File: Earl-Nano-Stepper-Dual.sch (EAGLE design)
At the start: 25 parts, among them IC1 ULN2003AN, J4 CONNECTOR-M03254-LOCK, M1 ARDUINO-NANO-3.0, SW1 PB1, SW2 PB2, SW3 Toggle 1

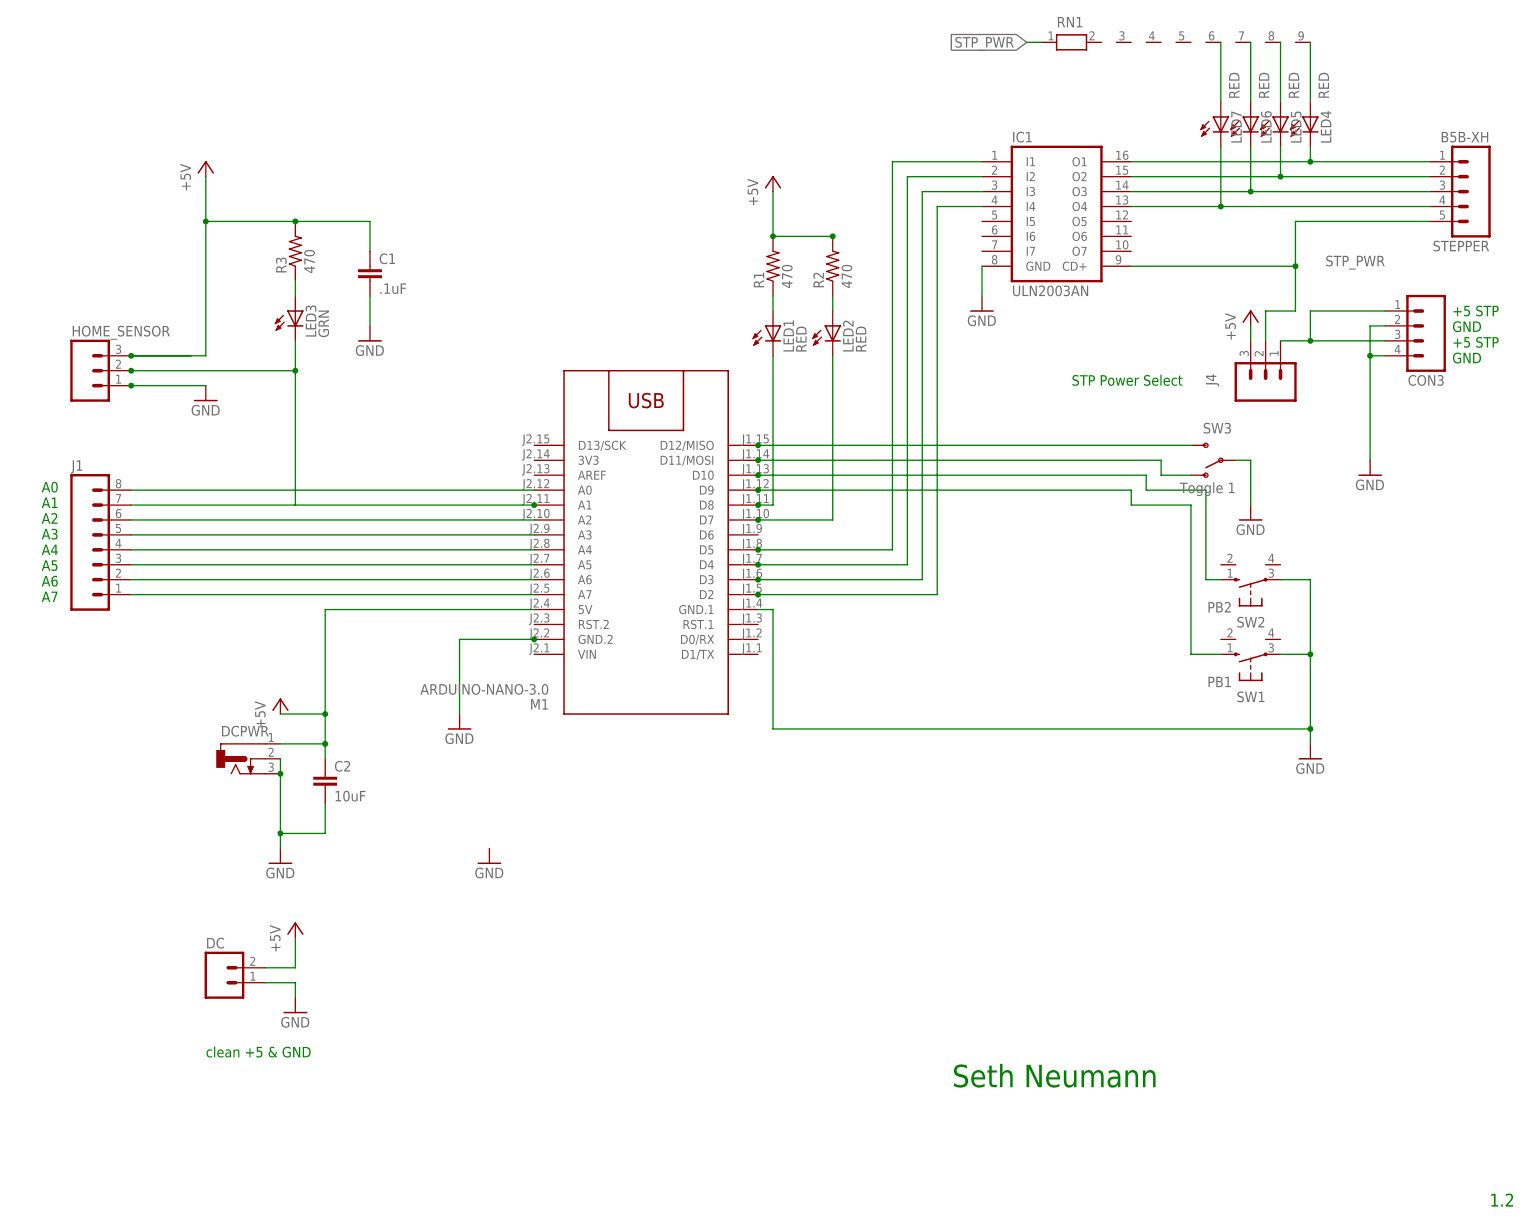
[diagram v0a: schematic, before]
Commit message: changes to support two stepper motors
changed to ULN2803
Moved both home sensors to A6,A7
Added LEDs, 2nd connector etc
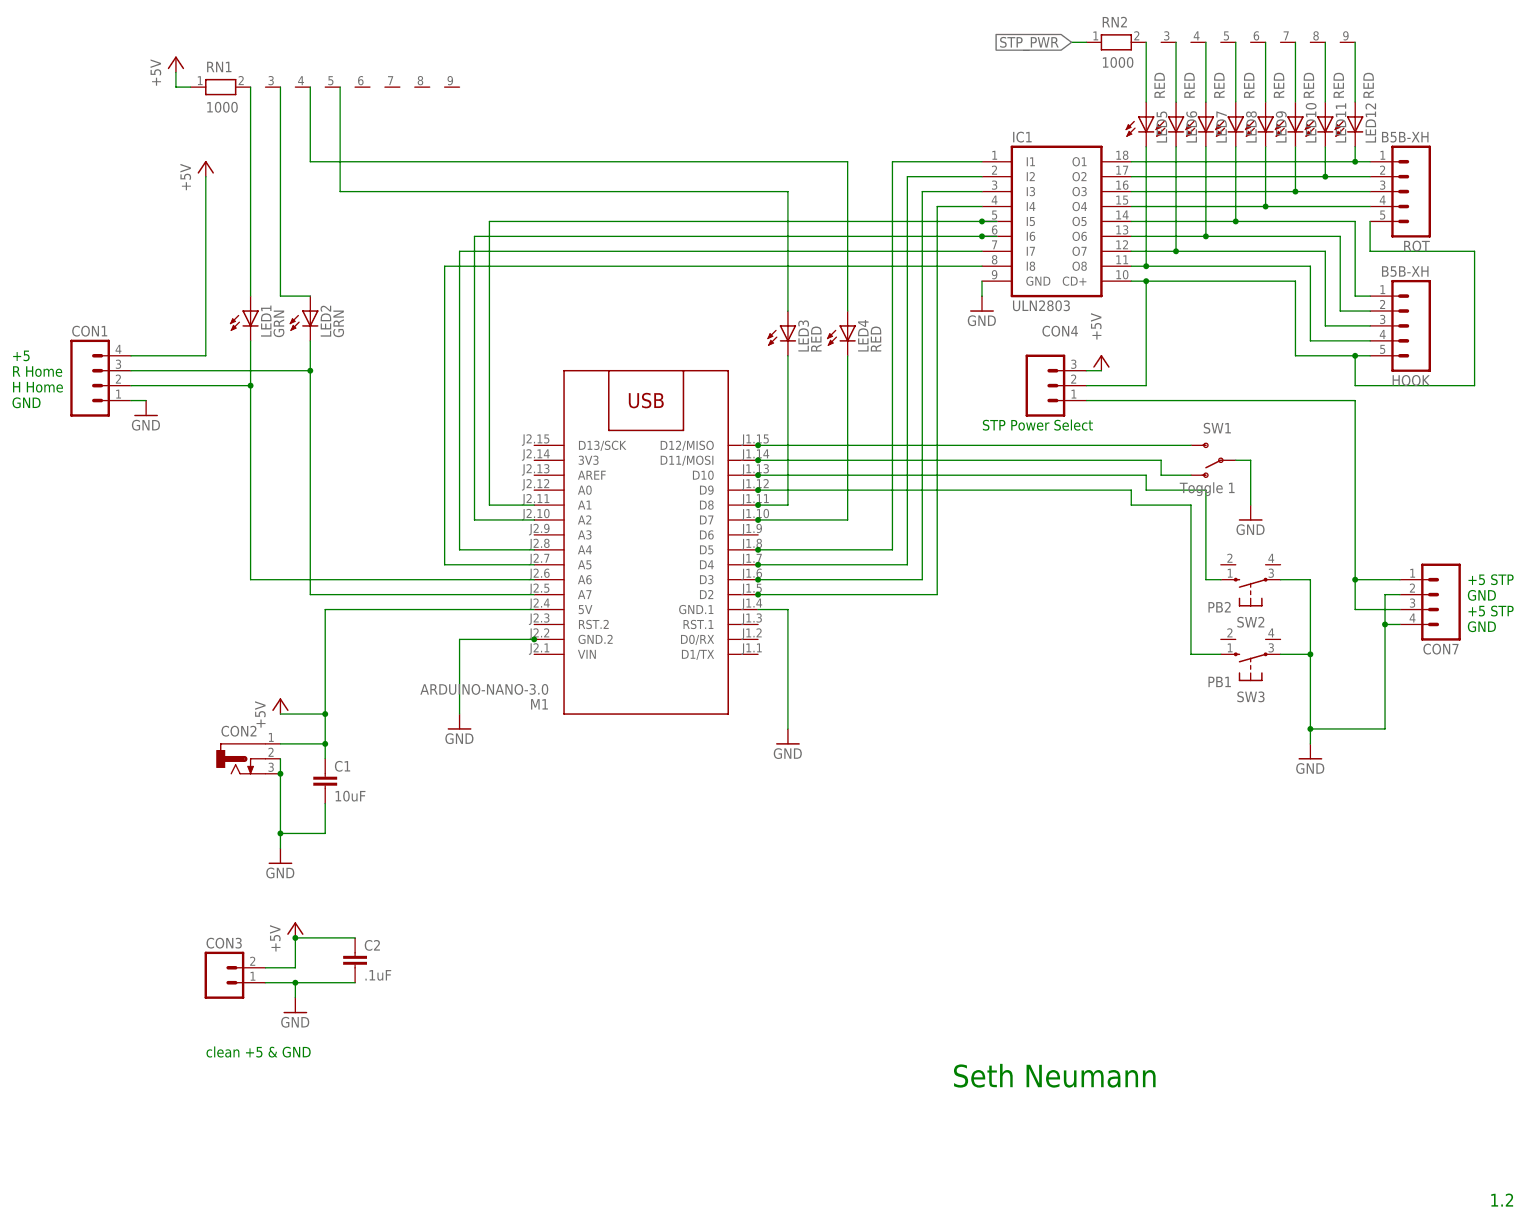
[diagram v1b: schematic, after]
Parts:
- removed DC: (no value), SPCoast:CONNECTOR-M02350-LOCK
- removed HOME_SENSOR, J4: CONNECTOR-M03254-LOCK, SPCoast:CONNECTOR-M03254-LOCK
- removed J1: (no value), SPCoast:CONNECTOR-M08LOCK
- removed R1, R2, R3: 470, SPCoast:RPTH04
- removed STEPPER: B5B-XH, SPCoast:CONNECTOR-M05LOCK
- added CON1: (no value), SPCoast:CONNECTOR-M04LOCK
- added CON4: CONNECTOR-M03254-LOCK, SPCoast:CONNECTOR-M03254-LOCK
- added CON7: (no value), SPCoast:CONNECTOR-M04SCREW_LOCK
- added HOOK, ROT: B5B-XH, SPCoast:CONNECTOR-M05LOCK
- added LED10, LED11, LED12, LED8, LED9: RED, SPCoast:LEDLED3MM
- added RN2: 1000, resistor-net:RN08
- C1: value .1uF -> 10uF
- C2: value 10uF -> .1uF
- CON3: device SPCoast:CONNECTOR-M04SCREW_LOCK -> SPCoast:CONNECTOR-M02350-LOCK
- IC1: value ULN2003AN -> ULN2803; device uln-udn:ULN2003AN -> uln-udn:ULN2803A
- LED1, LED2: value RED -> GRN
- LED3: value GRN -> RED
- RN1: value (none) -> 1000
- SW1: value PB1 -> Toggle 1; device SPCoast:SWITCH-(ON)SMALLPADS -> SPCoast:SWITCH-SPSTPTH-508
- SW3: value Toggle 1 -> PB1; device SPCoast:SWITCH-SPSTPTH-508 -> SPCoast:SWITCH-(ON)SMALLPADS
- renumbered DCPWR to CON2
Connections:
- removed net A1: HOME_SENSOR.2, J1.7, LED3.C, M1.A1
- new net N$28: CON4.1, CON7.1, CON7.3
- new net N$31: LED6.A, RN2.3
- new net N$32: HOOK.1, IC1.O5, LED8.C
- new net N$33: HOOK.2, IC1.O6, LED7.C
- new net N$34: HOOK.3, IC1.O7, LED6.C
- new net N$35: HOOK.4, IC1.O8, LED5.C
- new net N$36: LED7.A, RN2.4
- new net N$37: LED8.A, RN2.5
- net +5V: now also CON1.4, CON3.B, CON4.3, RN1.1; no longer DC.B, HOME_SENSOR.3, J4.3, R1.2, R2.2, R3.2
- net GND: now also CON1.1, CON3.A, CON7.2, CON7.4; no longer CON3.2, CON3.4, DC.A, HOME_SENSOR.1
- net N$1: now also LED12.C, ROT.1; no longer LED4.C, STEPPER.1
- net N$10: now also LED2.A, RN1.3; no longer LED3.A, R3.1
- net N$15: now also LED11.C, ROT.2; no longer LED5.C, STEPPER.2
- net N$16: now also LED10.C, ROT.3; no longer LED6.C, STEPPER.3
- net N$17: now also LED9.C, ROT.4; no longer LED7.C, STEPPER.4
- net N$18: now also LED9.A, RN2.6; no longer LED7.A, RN1.6
- net N$19: now also CON1.3, LED2.C, M1.A7; no longer CON3.1, CON3.3, J4.1
- net N$2: now also SW1.S; no longer SW3.S
- net N$20: now also LED10.A, RN2.7; no longer LED6.A, RN1.7
- net N$21: now also LED11.A, RN2.8; no longer LED5.A, RN1.8
- net N$22: now also LED12.A, RN2.9; no longer LED4.A, RN1.9
- net N$23: now also IC1.I5, M1.A1; no longer J1.8, M1.A0
- net N$24: now also IC1.I6; no longer J1.6
- net N$25: now also IC1.I7, M1.A4; no longer J1.5, M1.A3
- net N$26: now also IC1.I8, M1.A5; no longer J1.4, M1.A4
- net N$27: now also LED5.A, RN2.2; no longer J1.3, M1.A5
- net N$29: now also CON1.2, LED1.C; no longer J1.2
- net N$3: now also SW1.O; no longer SW3.O
- net N$30: now also LED1.A, RN1.2; no longer J1.1, M1.A7
- net N$5: now also SW3.S; no longer SW1.S
- net N$6: now also LED3.C; no longer LED1.C
- net N$7: now also LED4.C; no longer LED2.C
- net N$8: now also LED3.A, RN1.5; no longer LED1.A, R1.1
- net N$9: now also LED4.A, RN1.4; no longer LED2.A, R2.1
- net STP_PWR: now also CON4.2, HOOK.5, RN2.1, ROT.5; no longer J4.2, RN1.1, STEPPER.5
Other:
- note added: "+5 R Home H Home GND"
- note removed: "A0 A1 A2 A3 A4 A5 A6 A7"
- moved on the sheet: C1, C2, LED1, LED2, LED3, LED4, LED5, LED6, LED7, RN1

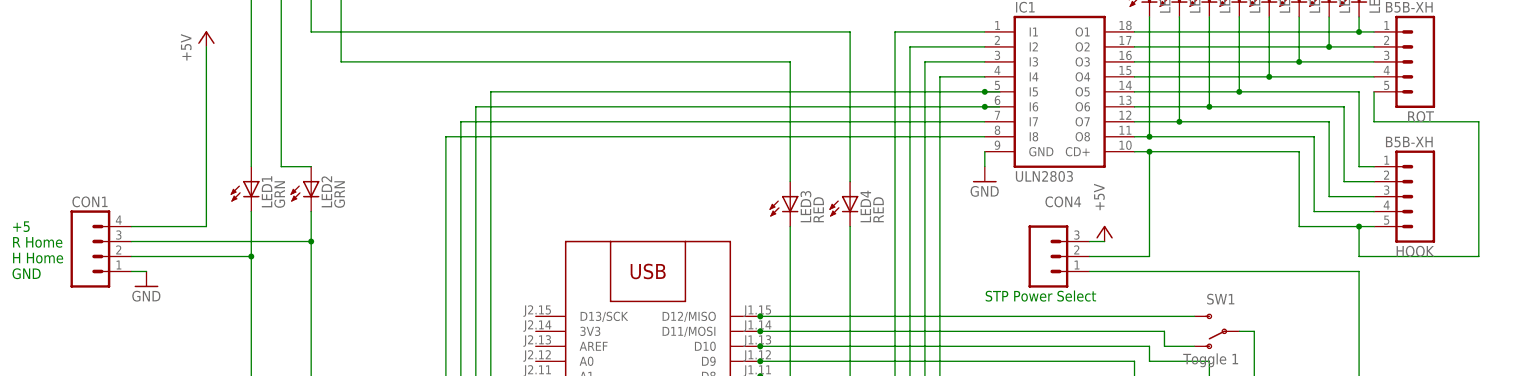
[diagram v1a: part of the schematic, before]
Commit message: changes resulting initial board order
changes resulting in initial board order
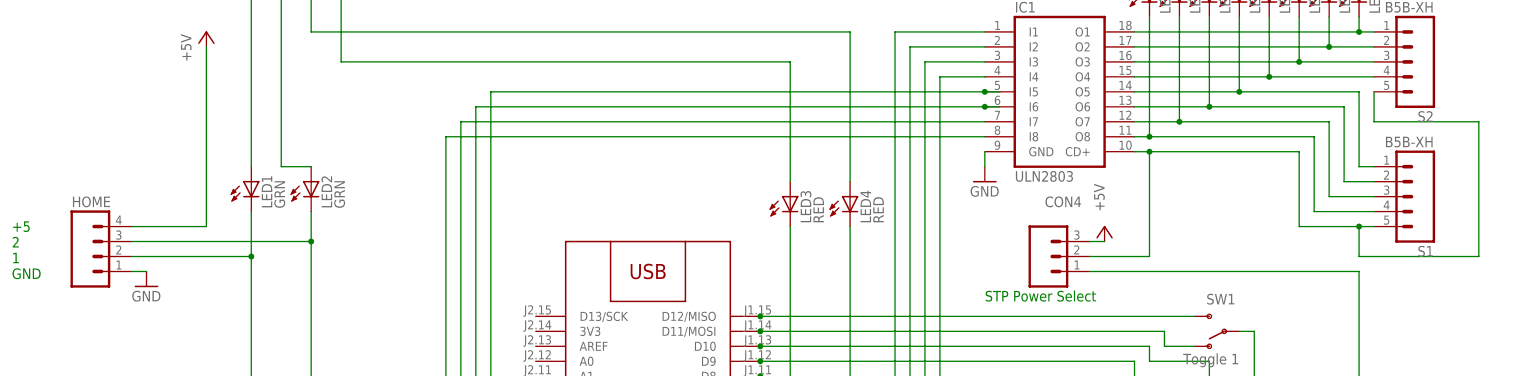
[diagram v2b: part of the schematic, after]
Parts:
- renumbered CON1 to HOME, HOOK to S1, ROT to S2
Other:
- note added: "+5 2 1 GND"
- note removed: "+5 R Home H Home GND"
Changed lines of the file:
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@@
 <part name="GND3" library="SPCoast" deviceset="GND" device=""/>
 <part name="GND6" library="SPCoast" deviceset="GND" device=""/>
-<part name="ROT" library="SPCoast" deviceset="CONNECTOR-M05" device="LOCK" value="B5B-XH"/>
+<part name="S2" library="SPCoast" deviceset="CONNECTOR-M05" device="LOCK" value="B5B-XH"/>
 <part name="CON4" library="SPCoast" deviceset="CONNECTOR-M03" device="254-LOCK" value="CONNECTOR-M03254-LOCK"/>
 <part name="RN2" library="resistor-net" deviceset="RN08" device="" value="1000"/>
@@
 <part name="CON7" library="SPCoast" deviceset="CONNECTOR-M04" device="SCREW_LOCK"/>
 <part name="IC1" library="uln-udn" deviceset="ULN2803A" device="" value="ULN2803"/>
-<part name="CON1" library="SPCoast" deviceset="CONNECTOR-M04" device="LOCK"/>
+<part name="HOME" library="SPCoast" deviceset="CONNECTOR-M04" device="LOCK"/>
 <part name="LED1" library="SPCoast" deviceset="LED*" device="LED3MM" value="GRN"/>
-<part name="HOOK" library="SPCoast" deviceset="CONNECTOR-M05" device="LOCK" value="B5B-XH"/>
+<part name="S1" library="SPCoast" deviceset="CONNECTOR-M05" device="LOCK" value="B5B-XH"/>
 <part name="LED8" library="SPCoast" deviceset="LED*" device="LED3MM" value="RED"/>
 <part name="LED7" library="SPCoast" deviceset="LED*" device="LED3MM" value="RED"/>
@@
 <text x="180.34" y="139.7" size="1.778" layer="91">STP Power Select</text>
 <text x="15.24" y="143.51" size="1.778" layer="91">+5
-R Home
-H Home
+2
+1
 GND</text>
 </plain>
@@
 <instance part="GND3" gate="1" x="63.5" y="40.64"/>
 <instance part="GND6" gate="1" x="180.34" y="160.02"/>
-<instance part="ROT" gate="CON1" x="254" y="180.34" rot="R180"/>
+<instance part="S2" gate="CON1" x="254" y="180.34" rot="R180"/>
 <instance part="CON4" gate="G$1" x="191.77" y="147.32" smashed="yes">
 <attribute name="NAME" x="190.5" y="155.702" size="1.778" layer="95"/>
@@
 <instance part="CON7" gate="J" x="256.54" y="111.76" rot="R180"/>
 <instance part="IC1" gate="G$1" x="193.04" y="175.26"/>
-<instance part="CON1" gate="J" x="30.48" y="147.32"/>
+<instance part="HOME" gate="J" x="30.48" y="147.32"/>
 <instance part="LED1" gate="LED" x="55.88" y="157.48"/>
-<instance part="HOOK" gate="CON1" x="254" y="157.48" rot="R180"/>
+<instance part="S1" gate="CON1" x="254" y="157.48" rot="R180"/>
 <instance part="LED8" gate="LED" x="223.52" y="190.5" smashed="yes">
 <attribute name="NAME" x="227.076" y="188.468" size="1.778" layer="95" rot="R90"/>
@@
 <segment>
 <pinref part="GND1" gate="1" pin="GND"/>
-<pinref part="CON1" gate="J" pin="1"/>
+<pinref part="HOME" gate="J" pin="1"/>
 <wire x1="38.1" y1="144.78" x2="35.56" y2="144.78" width="0.4064" layer="91"/>
 </segment>
@@
 <pinref part="P+2" gate="1" pin="+5V"/>
 <wire x1="48.26" y1="182.88" x2="48.26" y2="152.4" width="0.6096" layer="91"/>
-<pinref part="CON1" gate="J" pin="4"/>
+<pinref part="HOME" gate="J" pin="4"/>
 <wire x1="48.26" y1="152.4" x2="35.56" y2="152.4" width="0.4064" layer="91"/>
 </segment>
@@
 <net name="N$1" class="0">
 <segment>
-<pinref part="ROT" gate="CON1" pin="1"/>
+<pinref part="S2" gate="CON1" pin="1"/>
 <wire x1="205.74" y1="185.42" x2="243.84" y2="185.42" width="0.3048" layer="91"/>
 <pinref part="LED12" gate="LED" pin="C"/>
@@
 <net name="N$15" class="0">
 <segment>
-<pinref part="ROT" gate="CON1" pin="2"/>
+<pinref part="S2" gate="CON1" pin="2"/>
 <wire x1="205.74" y1="182.88" x2="238.76" y2="182.88" width="0.3048" layer="91"/>
 <pinref part="LED11" gate="LED" pin="C"/>
@@
 <net name="N$16" class="0">
 <segment>
-<pinref part="ROT" gate="CON1" pin="3"/>
+<pinref part="S2" gate="CON1" pin="3"/>
 <wire x1="205.74" y1="180.34" x2="233.68" y2="180.34" width="0.3048" layer="91"/>
 <pinref part="LED10" gate="LED" pin="C"/>
@@
 <net name="N$17" class="0">
 <segment>
-<pinref part="ROT" gate="CON1" pin="4"/>
+<pinref part="S2" gate="CON1" pin="4"/>
 <wire x1="205.74" y1="177.8" x2="228.6" y2="177.8" width="0.3048" layer="91"/>
 <pinref part="LED9" gate="LED" pin="C"/>
@@
 <junction x="208.28" y="165.1"/>
 <wire x1="233.68" y1="165.1" x2="233.68" y2="152.4" width="0.4064" layer="91"/>
-<pinref part="HOOK" gate="CON1" pin="5"/>
+<pinref part="S1" gate="CON1" pin="5"/>
 <wire x1="233.68" y1="152.4" x2="243.84" y2="152.4" width="0.4064" layer="91"/>
 <wire x1="243.84" y1="152.4" x2="246.38" y2="152.4" width="0.4064" layer="91"/>
@@
 <wire x1="264.16" y1="147.32" x2="264.16" y2="170.18" width="0.4064" layer="91"/>
 <wire x1="264.16" y1="170.18" x2="246.38" y2="170.18" width="0.4064" layer="91"/>
-<pinref part="ROT" gate="CON1" pin="5"/>
+<pinref part="S2" gate="CON1" pin="5"/>
 <wire x1="246.38" y1="170.18" x2="246.38" y2="175.26" width="0.4064" layer="91"/>
 <junction x="243.84" y="152.4"/>
@@
 <segment>
 <pinref part="M1" gate="G$1" pin="A6"/>
-<pinref part="CON1" gate="J" pin="2"/>
+<pinref part="HOME" gate="J" pin="2"/>
 <wire x1="55.88" y1="114.3" x2="104.14" y2="114.3" width="0.3048" layer="91"/>
 <wire x1="35.56" y1="147.32" x2="55.88" y2="147.32" width="0.3048" layer="91"/>
@@
 <wire x1="66.04" y1="154.94" x2="66.04" y2="149.86" width="0.3048" layer="91"/>
 <wire x1="35.56" y1="149.86" x2="66.04" y2="149.86" width="0.3048" layer="91"/>
-<pinref part="CON1" gate="J" pin="3"/>
+<pinref part="HOME" gate="J" pin="3"/>
 <pinref part="M1" gate="G$1" pin="A7"/>
 <wire x1="66.04" y1="111.76" x2="104.14" y2="111.76" width="0.3048" layer="91"/>
@@
 <wire x1="243.84" y1="175.26" x2="243.84" y2="162.56" width="0.3048" layer="91"/>
 <wire x1="243.84" y1="162.56" x2="246.38" y2="162.56" width="0.3048" layer="91"/>
-<pinref part="HOOK" gate="CON1" pin="1"/>
+<pinref part="S1" gate="CON1" pin="1"/>
 <pinref part="LED8" gate="LED" pin="C"/>
 <wire x1="223.52" y1="187.96" x2="223.52" y2="175.26" width="0.3048" layer="91"/>
@@
 <wire x1="218.44" y1="172.72" x2="241.3" y2="172.72" width="0.3048" layer="91"/>
 <wire x1="241.3" y1="172.72" x2="241.3" y2="160.02" width="0.3048" layer="91"/>
-<pinref part="HOOK" gate="CON1" pin="2"/>
+<pinref part="S1" gate="CON1" pin="2"/>
 <wire x1="241.3" y1="160.02" x2="246.38" y2="160.02" width="0.3048" layer="91"/>
 <pinref part="LED7" gate="LED" pin="C"/>
@@
 <wire x1="213.36" y1="170.18" x2="238.76" y2="170.18" width="0.3048" layer="91"/>
 <wire x1="238.76" y1="170.18" x2="238.76" y2="157.48" width="0.3048" layer="91"/>
-<pinref part="HOOK" gate="CON1" pin="3"/>
+<pinref part="S1" gate="CON1" pin="3"/>
 <wire x1="238.76" y1="157.48" x2="246.38" y2="157.48" width="0.3048" layer="91"/>
 <pinref part="LED6" gate="LED" pin="C"/>
@@
 <wire x1="208.28" y1="167.64" x2="236.22" y2="167.64" width="0.3048" layer="91"/>
 <wire x1="236.22" y1="167.64" x2="236.22" y2="154.94" width="0.3048" layer="91"/>
-<pinref part="HOOK" gate="CON1" pin="4"/>
+<pinref part="S1" gate="CON1" pin="4"/>
 <wire x1="236.22" y1="154.94" x2="246.38" y2="154.94" width="0.3048" layer="91"/>
 <pinref part="LED5" gate="LED" pin="C"/>
